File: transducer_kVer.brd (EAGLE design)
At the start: 33 x 33 mm, 12 parts, among them U1 ADS1014IDGST

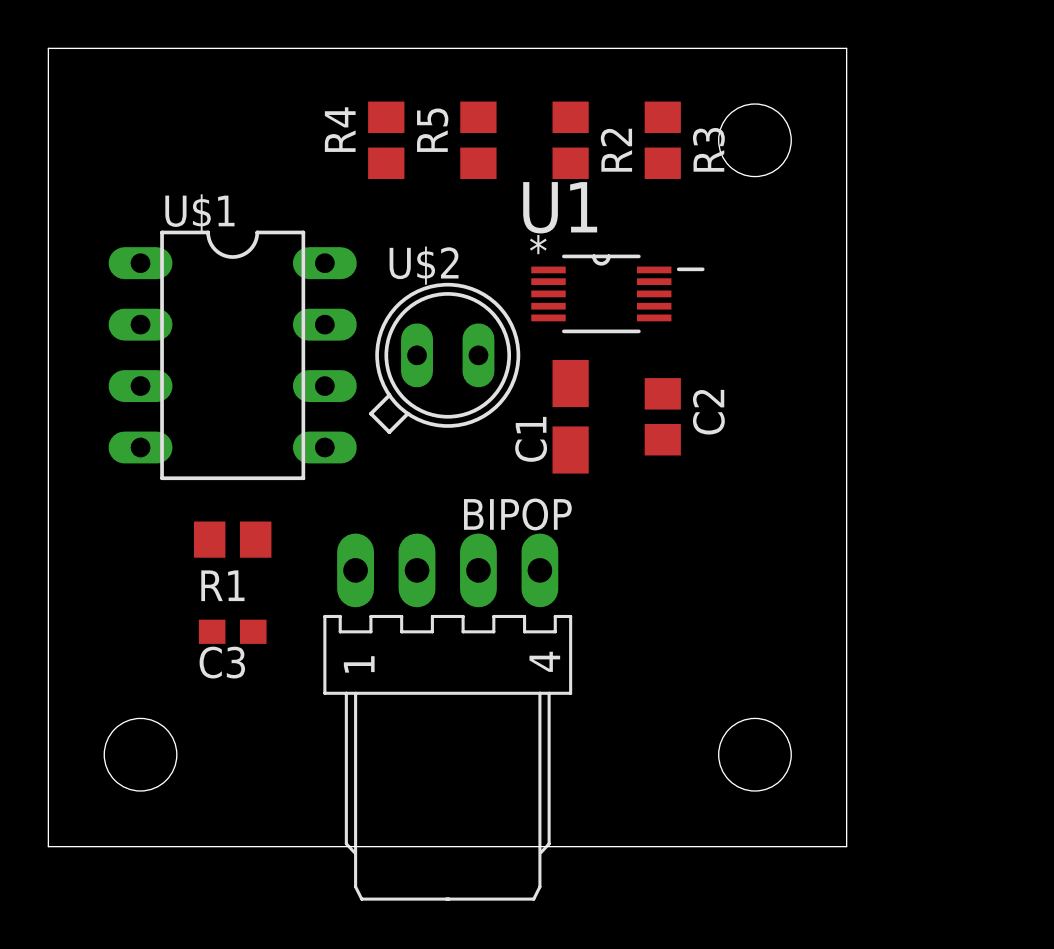
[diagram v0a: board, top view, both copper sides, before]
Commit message: BIPOP board redesigned, new versions of transducers added.
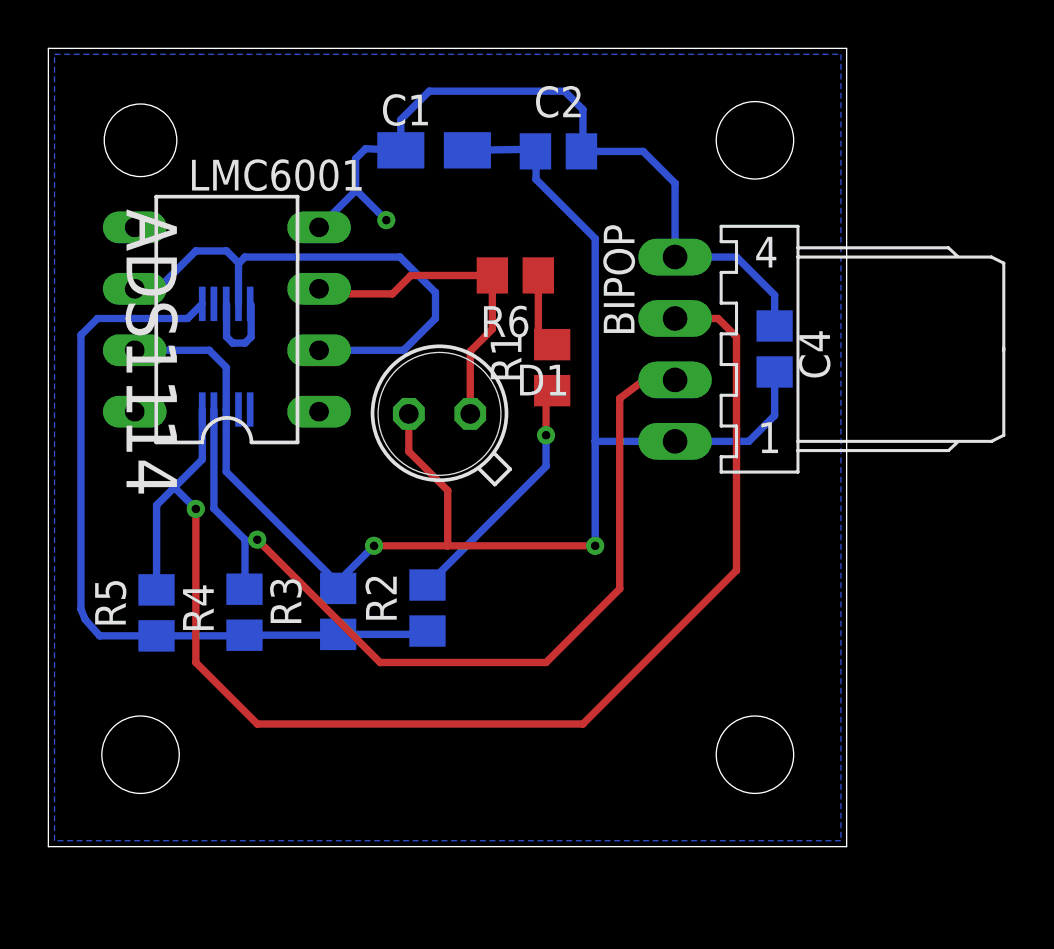
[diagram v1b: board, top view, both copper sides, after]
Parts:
- removed C3: 10pF, rcl:C0603
- removed U$1: LMC6001, customy:DIL08
- removed U$2: BPW21, customy:TO52
- removed U1: ADS1014IDGST, Texas Instruments_By_element14_Batch_1:SOP50P490X110-10N
- added ADS1114: ADS1014IDGST, Texas Instruments_By_element14_Batch_1:SOP50P490X110-10N
- added C4: 4.7µ, rcl:C0805
- added D1: (no value), diode:TO18D
- added LMC6001: LMC6001, customy:DIL08
- added R6: 3M, rcl:R0805
- R1: value 1M -> 3M
- moved R3 23.7 mm to (12.0, 56.7), flipped to the bottom, turned to 90 degrees
- moved R5 23.6 mm to (4.47, 56.7), flipped to the bottom
- moved R4 20.4 mm to (8.11, 56.7), flipped to the bottom
- moved R2 20.2 mm to (15.7, 56.9), flipped to the bottom, turned to 90 degrees
- moved R1 15.0 mm to (20.8, 66.8), turned to 90 degrees
- moved BIPOP 13.1 mm to (25.9, 67.6), turned to 270 degrees
- moved C1 12.4 mm to (15.9, 75.8), flipped to the bottom, turned to 180 degrees
- moved C2 11.8 mm to (21.1, 75.7), flipped to the bottom, turned to 180 degrees
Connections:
- removed net 3.3V: BIPOP.1, C1.+, C2.1, R3.2, U$1.7, U1.8
- removed net N$5: C3.1, R1.1, U$1.2, U$2.2
- new net 5V: ADS1114.8, BIPOP.1, C1.+, C2.1, C4.1, D1.C, LMC6001.7, R3.2
- new net ADR: ADS1114.1, R2.1, R3.1, R4.1, R5.1
- new net N$2: R1.2, R6.1
- net GND: now also ADS1114.3, ADS1114.5, C4.2, LMC6001.4, R1.1; no longer U$1.3, U$1.4, U$2.1, U1.3, U1.5
- net N$3: now also D1.A, LMC6001.3, R6.2; no longer R2.1, R3.1, R4.1, R5.1, U1.1
- net N$8: now also ADS1114.2; no longer U1.2
- net SCL: now also ADS1114.10; no longer U1.10
- net SDA: now also ADS1114.9; no longer U1.9
- net U_OUT: now also ADS1114.4, LMC6001.2, LMC6001.6; no longer C3.2, R1.2, U$1.6, U1.4
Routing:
- net 5V: track 0.00 -> 62.3 mm, vias 0 -> 2
- net SCL: track 0.00 -> 54.4 mm, vias 0 -> 1
- net GND: track 0.00 -> 46.7 mm, vias 0 -> 2
- net SDA: track 0.00 -> 37.2 mm, vias 0 -> 1
- net ADR: track 0.00 -> 31.9 mm
- net U_OUT: track 0.00 -> 22.1 mm
- net N$3: track 0.00 -> 13.7 mm
- net N$2: track 0.00 -> 3.10 mm
- added copper zone on layer 16, net GND
